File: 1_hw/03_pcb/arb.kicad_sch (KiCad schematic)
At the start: 0 parts

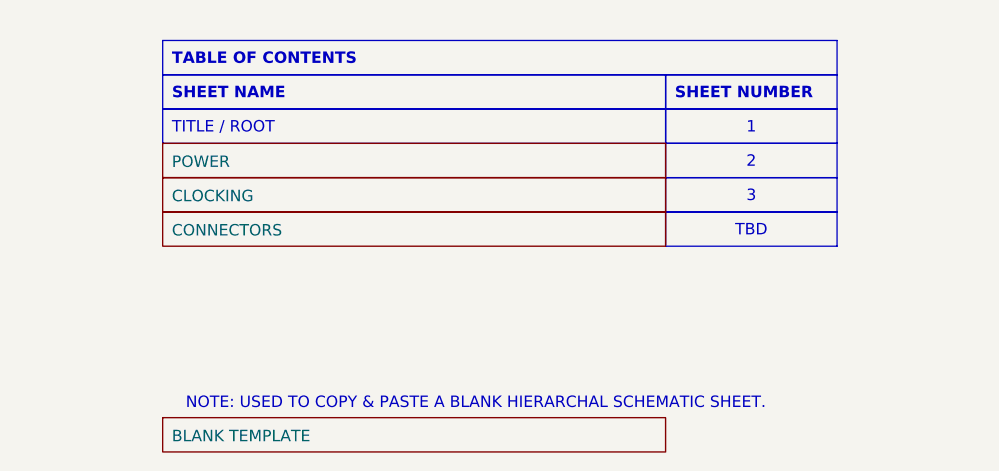
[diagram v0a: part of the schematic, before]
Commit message: FEAT: Modified Block Diagram. Added Pin Map Excel.
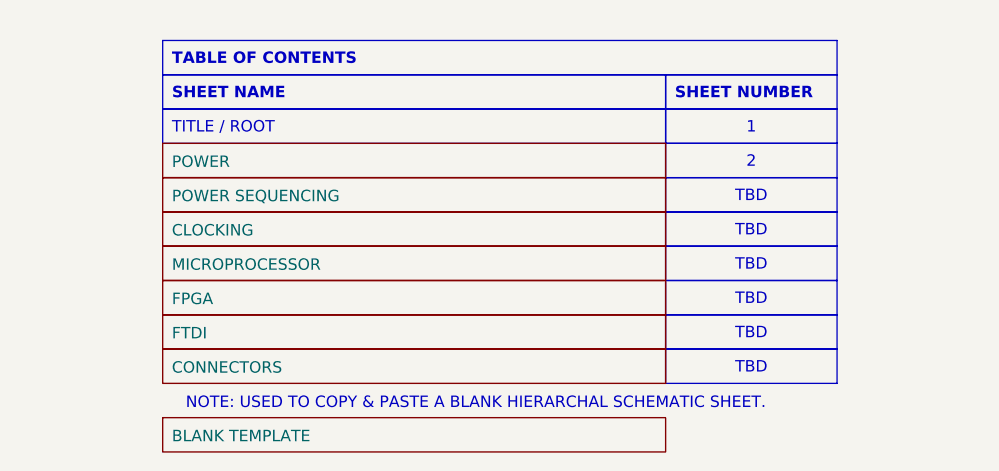
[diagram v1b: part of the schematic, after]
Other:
- added sheet FPGA (fpga.kicad_sch)
- added sheet FTDI (ftdi.kicad_sch)
- added sheet MICROPROCESSOR (microprocessor.kicad_sch)
- added sheet POWER SEQUENCING (power_seq.kicad_sch)
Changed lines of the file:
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@@
 		(rev "0.0.1")
 		(company "Tomasz Brzyzek")
-		(comment 1 "brzk.net")
+		(comment 1 "Stasia Brzyzek")
 	)
 	(text_box "2"
@@
 		)
 	)
-	(text_box "3"
-		(exclude_from_sim no)
-		(at 165.1 85.09 0)
+	(text_box "TBD"
+		(exclude_from_sim no)
+		(at 165.1 88.9 0)
 		(size 19.05 3.81)
 		(stroke
@@
 		)
 	)
+	(text_box "TBD"
+		(exclude_from_sim no)
+		(at 165.1 92.71 0)
+		(size 19.05 3.81)
+		(stroke
+			(width 0)
+			(type default)
+			(color 0 0 0 1)
+		)
+		(fill
+			(type none)
+		)
+		(effects
+			(font
+				(size 1.27 1.27)
+				(color 0 72 72 1)
+			)
+		)
+	)
 	(text_box "SHEET NAME"
 		(exclude_from_sim no)
@@
 	(text_box "TBD"
 		(exclude_from_sim no)
-		(at 165.1 88.9 0)
+		(at 165.1 104.14 0)
 		(size 19.05 3.81)
 		(stroke
@@
 		)
 	)
+	(text_box "TBD"
+		(exclude_from_sim no)
+		(at 165.1 100.33 0)
+		(size 19.05 3.81)
+		(stroke
+			(width 0)
+			(type default)
+			(color 0 0 0 1)
+		)
+		(fill
+			(type none)
+		)
+		(effects
+			(font
+				(size 1.27 1.27)
+				(color 0 72 72 1)
+			)
+		)
+	)
+	(text_box "TBD"
+		(exclude_from_sim no)
+		(at 165.1 85.09 0)
+		(size 19.05 3.81)
+		(stroke
+			(width 0)
+			(type default)
+			(color 0 0 0 1)
+		)
+		(fill
+			(type none)
+		)
+		(effects
+			(font
+				(size 1.27 1.27)
+				(color 0 72 72 1)
+			)
+		)
+	)
 	(text_box "NOTES:\n1.	TBD"
 		(exclude_from_sim no)
@@
 		)
 	)
+	(text_box "TBD"
+		(exclude_from_sim no)
+		(at 165.1 96.52 0)
+		(size 19.05 3.81)
+		(stroke
+			(width 0)
+			(type default)
+			(color 0 0 0 1)
+		)
+		(fill
+			(type none)
+		)
+		(effects
+			(font
+				(size 1.27 1.27)
+				(color 0 72 72 1)
+			)
+		)
+	)
 	(text_box "1"
 		(exclude_from_sim no)
@@
 			(font
 				(size 1.27 1.27)
+			)
+		)
+	)
+	(sheet
+		(at 109.22 92.71)
+		(size 55.88 3.81)
+		(stroke
+			(width 0.1524)
+			(type solid)
+			(color 0 0 0 1)
+		)
+		(fill
+			(color 0 0 0 0.0000)
+		)
+		(property "Sheetname" "MICROPROCESSOR"
+			(at 110.236 94.742 0)
+			(effects
+				(font
+					(size 1.27 1.27)
+				)
+				(justify left)
+			)
+		)
+		(property "Sheetfile" "microprocessor.kicad_sch"
+			(at 109.22 97.1046 0)
+			(effects
+				(font
+					(size 1.27 1.27)
+				)
+				(justify left top)
+				(hide yes)
+			)
+		)
+		(instances
+			(project "arb"
+				(path "/866ef9be-3b01-4288-a6e0-a2357aa17e50"
+					(page "5")
+				)
+			)
+		)
+	)
+	(sheet
+		(at 109.22 96.52)
+		(size 55.88 3.81)
+		(stroke
+			(width 0.1524)
+			(type solid)
+			(color 0 0 0 1)
+		)
+		(fill
+			(color 0 0 0 0.0000)
+		)
+		(property "Sheetname" "FPGA"
+			(at 110.236 98.552 0)
+			(effects
+				(font
+					(size 1.27 1.27)
+				)
+				(justify left)
+			)
+		)
+		(property "Sheetfile" "fpga.kicad_sch"
+			(at 109.22 100.9146 0)
+			(effects
+				(font
+					(size 1.27 1.27)
+				)
+				(justify left top)
+				(hide yes)
+			)
+		)
+		(instances
+			(project "arb"
+				(path "/866ef9be-3b01-4288-a6e0-a2357aa17e50"
+					(page "6")
+				)
 			)
 		)
@@
 			(color 0 0 0 0.0000)
 		)
+		(property "Sheetname" "POWER SEQUENCING"
+			(at 110.236 87.122 0)
+			(effects
+				(font
+					(size 1.27 1.27)
+				)
+				(justify left)
+			)
+		)
+		(property "Sheetfile" "power_seq.kicad_sch"
+			(at 109.22 89.4846 0)
+			(effects
+				(font
+					(size 1.27 1.27)
+				)
+				(justify left top)
+				(hide yes)
+			)
+		)
+		(instances
+			(project "arb"
+				(path "/866ef9be-3b01-4288-a6e0-a2357aa17e50"
+					(page "4")
+				)
+			)
+		)
+	)
+	(sheet
+		(at 109.22 88.9)
+		(size 55.88 3.81)
+		(stroke
+			(width 0.1524)
+			(type solid)
+			(color 0 0 0 1)
+		)
+		(fill
+			(color 0 0 0 0.0000)
+		)
 		(property "Sheetname" "CLOCKING"
-			(at 110.236 87.122 0)
+			(at 110.236 90.932 0)
 			(effects
 				(font
@@
 		)
 		(property "Sheetfile" "clocking.kicad_sch"
-			(at 109.22 89.4846 0)
+			(at 109.22 93.2946 0)
 			(effects
 				(font
@@
 				(path "/866ef9be-3b01-4288-a6e0-a2357aa17e50"
 					(page "3")
+				)
+			)
+		)
+	)
+	(sheet
+		(at 109.22 100.33)
+		(size 55.88 3.81)
+		(stroke
+			(width 0.1524)
+			(type solid)
+			(color 0 0 0 1)
+		)
+		(fill
+			(color 0 0 0 0.0000)
+		)
+		(property "Sheetname" "FTDI"
+			(at 110.236 102.362 0)
+			(effects
+				(font
+					(size 1.27 1.27)
+				)
+				(justify left)
+			)
+		)
+		(property "Sheetfile" "ftdi.kicad_sch"
+			(at 109.22 104.7246 0)
+			(effects
+				(font
+					(size 1.27 1.27)
+				)
+				(justify left top)
+				(hide yes)
+			)
+		)
+		(instances
+			(project "arb"
+				(path "/866ef9be-3b01-4288-a6e0-a2357aa17e50"
+					(page "7")
 				)
 			)
@@
 			(project "arb"
 				(path "/866ef9be-3b01-4288-a6e0-a2357aa17e50"
-					(page "4")
-				)
-			)
-		)
-	)
-	(sheet
-		(at 109.22 88.9)
+					(page "10")
+				)
+			)
+		)
+	)
+	(sheet
+		(at 109.22 104.14)
 		(size 55.88 3.81)
 		(stroke
@@
 		)
 		(property "Sheetname" "CONNECTORS"
-			(at 110.236 90.932 0)
+			(at 110.236 106.172 0)
 			(effects
 				(font
@@
 		)
 		(property "Sheetfile" "connectors.kicad_sch"
-			(at 109.22 93.2946 0)
-			(effects
-				(font
-					(size 1.27 1.27)
-				)
-				(justify left top)
-				(hide yes)
-			)
-		)
-		(instances
-			(project "arb"
-				(path "/866ef9be-3b01-4288-a6e0-a2357aa17e50"
-					(page "5")
-				)
-			)
+			(at 109.22 108.5346 0)
+			(effects
+				(font
+					(size 1.27 1.27)
+				)
+				(justify left top)
+				(hide yes)
+			)
+		)
+		(instances
+			(project "arb"
+				(path "/866ef9be-3b01-4288-a6e0-a2357aa17e50"
+					(page "9")
+				)
+			)

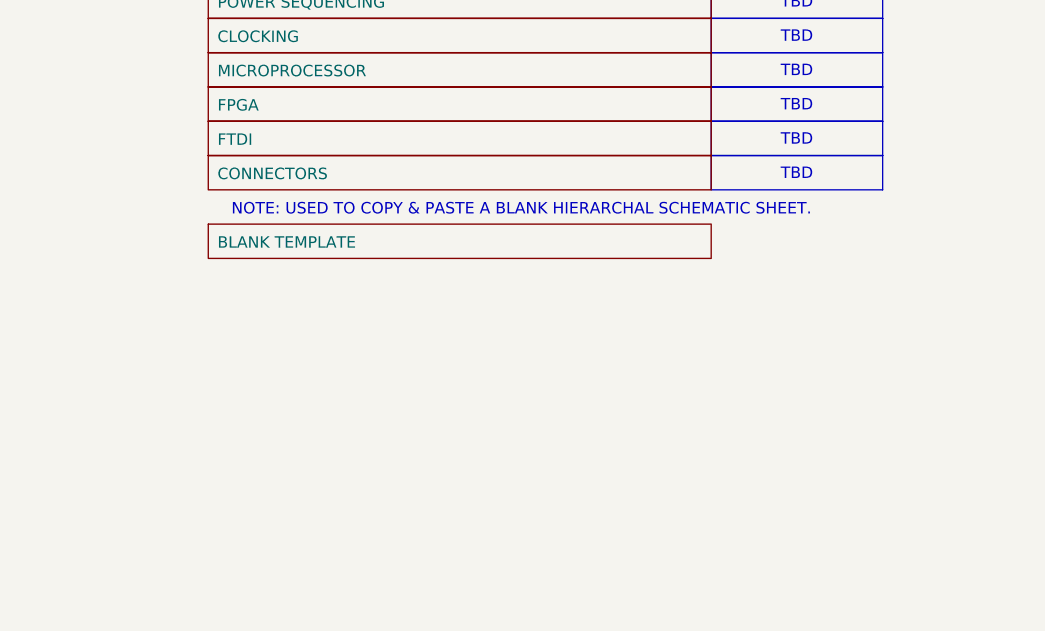
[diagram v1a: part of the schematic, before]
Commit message: FEAT: Added Level Translator Sheet, Symbols, added DAC and DDS to Schematic.
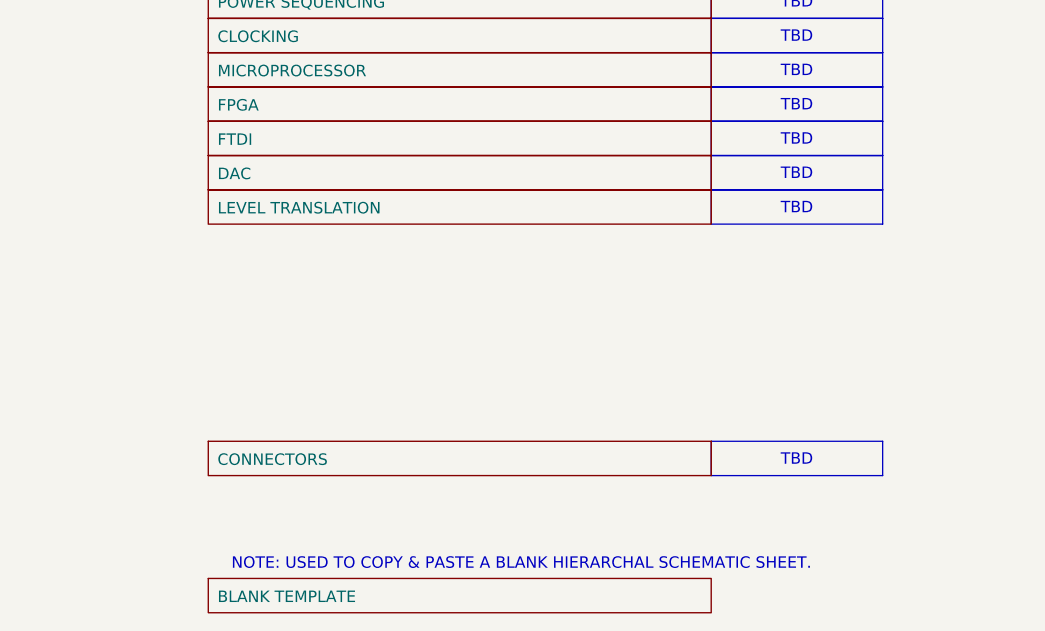
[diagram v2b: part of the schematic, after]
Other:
- added sheet DAC (dac.kicad_sch)
- added sheet LEVEL TRANSLATION (lvl_trns.kicad_sch)
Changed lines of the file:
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@@
+		)
+	)
+	(text_box "TBD"
+		(exclude_from_sim no)
+		(at 165.1 135.89 0)
+		(size 19.05 3.81)
+		(stroke
+			(width 0)
+			(type default)
+			(color 0 0 0 1)
+		)
+		(fill
+			(type none)
+		)
+		(effects
+			(font
+				(size 1.27 1.27)
+				(color 0 72 72 1)
+			)
+		)
+	)
+	(text_box "TBD"
+		(exclude_from_sim no)
+		(at 165.1 107.95 0)
+		(size 19.05 3.81)
+		(stroke
+			(width 0)
+			(type default)
+			(color 0 0 0 1)
+		)
+		(fill
+			(type none)
+		)
+		(effects
+			(font
+				(size 1.27 1.27)
+				(color 0 72 72 1)
+			)
 		)
 	)
@@
 	(text "NOTE: USED TO COPY & PASTE A BLANK HIERARCHAL SCHEMATIC SHEET."
 		(exclude_from_sim no)
-		(at 144.018 110.236 0)
+		(at 144.018 149.606 0)
 		(effects
 			(font
@@
 	)
 	(sheet
-		(at 109.22 111.76)
+		(at 109.22 104.14)
+		(size 55.88 3.81)
+		(stroke
+			(width 0.1524)
+			(type solid)
+			(color 0 0 0 1)
+		)
+		(fill
+			(color 0 0 0 0.0000)
+		)
+		(property "Sheetname" "DAC"
+			(at 110.236 106.172 0)
+			(effects
+				(font
+					(size 1.27 1.27)
+				)
+				(justify left)
+			)
+		)
+		(property "Sheetfile" "dac.kicad_sch"
+			(at 109.22 108.5346 0)
+			(effects
+				(font
+					(size 1.27 1.27)
+				)
+				(justify left top)
+				(hide yes)
+			)
+		)
+		(instances
+			(project "arb"
+				(path "/866ef9be-3b01-4288-a6e0-a2357aa17e50"
+					(page "8")
+				)
+			)
+		)
+	)
+	(sheet
+		(at 109.22 107.95)
+		(size 55.88 3.81)
+		(stroke
+			(width 0.1524)
+			(type solid)
+			(color 0 0 0 1)
+		)
+		(fill
+			(color 0 0 0 0.0000)
+		)
+		(property "Sheetname" "LEVEL TRANSLATION"
+			(at 110.236 109.982 0)
+			(effects
+				(font
+					(size 1.27 1.27)
+				)
+				(justify left)
+			)
+		)
+		(property "Sheetfile" "lvl_trns.kicad_sch"
+			(at 109.22 112.3446 0)
+			(effects
+				(font
+					(size 1.27 1.27)
+				)
+				(justify left top)
+				(hide yes)
+			)
+		)
+		(instances
+			(project "arb"
+				(path "/866ef9be-3b01-4288-a6e0-a2357aa17e50"
+					(page "9")
+				)
+			)
+		)
+	)
+	(sheet
+		(at 109.22 151.13)
 		(size 55.88 3.81)
 		(stroke
@@
 		)
 		(property "Sheetname" "BLANK TEMPLATE"
-			(at 110.236 113.792 0)
+			(at 110.236 153.162 0)
 			(effects
 				(font
@@
 		)
 		(property "Sheetfile" "blank_template.kicad_sch"
-			(at 109.22 116.1546 0)
-			(effects
-				(font
-					(size 1.27 1.27)
-				)
-				(justify left top)
-				(hide yes)
-			)
-		)
-		(instances
-			(project "arb"
-				(path "/866ef9be-3b01-4288-a6e0-a2357aa17e50"
-					(page "10")
-				)
-			)
-		)
-	)
-	(sheet
-		(at 109.22 104.14)
+			(at 109.22 155.5246 0)
+			(effects
+				(font
+					(size 1.27 1.27)
+				)
+				(justify left top)
+				(hide yes)
+			)
+		)
+		(instances
+			(project "arb"
+				(path "/866ef9be-3b01-4288-a6e0-a2357aa17e50"
+					(page "99")
+				)
+			)
+		)
+	)
+	(sheet
+		(at 109.22 135.89)
 		(size 55.88 3.81)
 		(stroke
@@
 		)
 		(property "Sheetname" "CONNECTORS"
-			(at 110.236 106.172 0)
+			(at 110.236 137.922 0)
 			(effects
 				(font
@@
 		)
 		(property "Sheetfile" "connectors.kicad_sch"
-			(at 109.22 108.5346 0)
-			(effects
-				(font
-					(size 1.27 1.27)
-				)
-				(justify left top)
-				(hide yes)
-			)
-		)
-		(instances
-			(project "arb"
-				(path "/866ef9be-3b01-4288-a6e0-a2357aa17e50"
-					(page "9")
-				)
-			)
+			(at 109.22 140.2846 0)
+			(effects
+				(font
+					(size 1.27 1.27)
+				)
+				(justify left top)
+				(hide yes)
+			)
+		)
+		(instances
+			(project "arb"
+				(path "/866ef9be-3b01-4288-a6e0-a2357aa17e50"
+					(page "20")
+				)
+			)

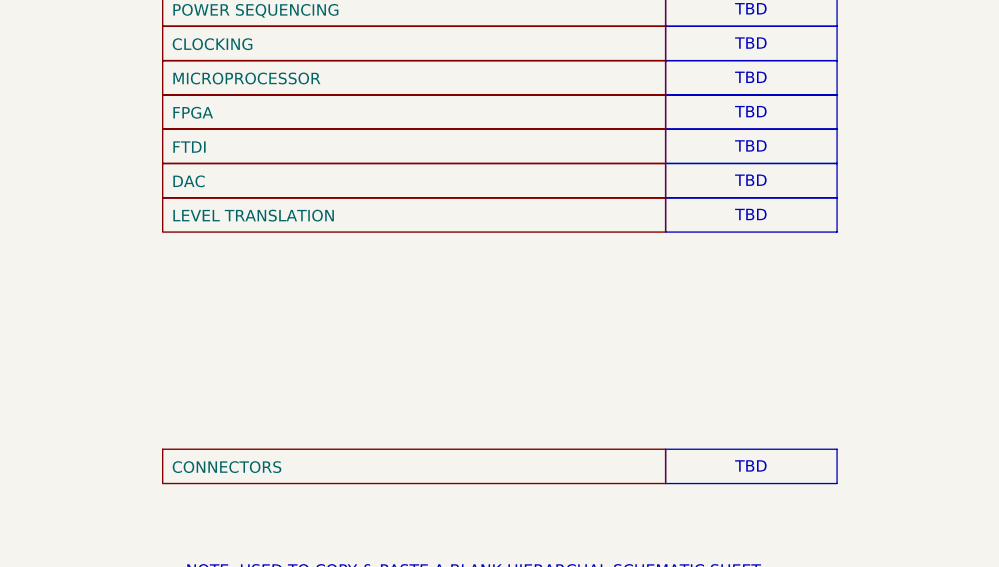
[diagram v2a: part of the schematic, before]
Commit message: FEAT: Simulated Analog Paths, added first stage analog amp to schematic.
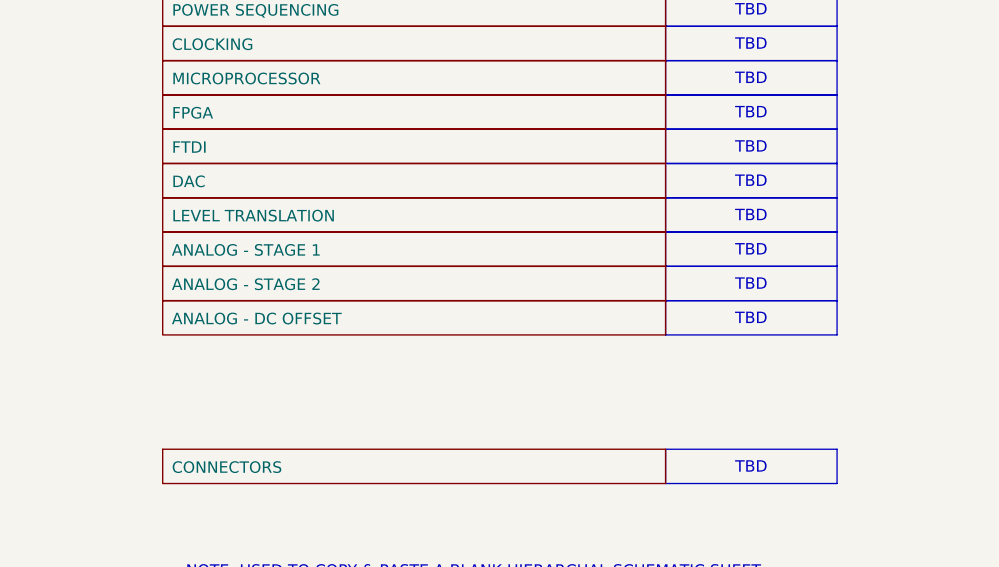
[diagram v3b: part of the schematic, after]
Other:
- added sheet ANALOG - DC OFFSET (analogdc.kicad_sch)
- added sheet ANALOG - STAGE 1 (analog1.kicad_sch)
- added sheet ANALOG - STAGE 2 (analog2.kicad_sch)
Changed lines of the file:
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@@
 		(rev "0.0.1")
 		(company "Tomasz Brzyzek")
-		(comment 1 "Stasia Brzyzek")
 	)
 	(text_box "2"
@@
 	(text_box "TBD"
 		(exclude_from_sim no)
+		(at 165.1 111.76 0)
+		(size 19.05 3.81)
+		(stroke
+			(width 0)
+			(type default)
+			(color 0 0 0 1)
+		)
+		(fill
+			(type none)
+		)
+		(effects
+			(font
+				(size 1.27 1.27)
+				(color 0 72 72 1)
+			)
+		)
+	)
+	(text_box "TBD"
+		(exclude_from_sim no)
 		(at 165.1 135.89 0)
 		(size 19.05 3.81)
@@
 		)
 	)
+	(text_box "TBD"
+		(exclude_from_sim no)
+		(at 165.1 119.38 0)
+		(size 19.05 3.81)
+		(stroke
+			(width 0)
+			(type default)
+			(color 0 0 0 1)
+		)
+		(fill
+			(type none)
+		)
+		(effects
+			(font
+				(size 1.27 1.27)
+				(color 0 72 72 1)
+			)
+		)
+	)
 	(text_box "INITIAL RELEASE"
 		(exclude_from_sim no)
@@
 		(exclude_from_sim no)
 		(at 165.1 77.47 0)
+		(size 19.05 3.81)
+		(stroke
+			(width 0)
+			(type default)
+			(color 0 0 0 1)
+		)
+		(fill
+			(type none)
+		)
+		(effects
+			(font
+				(size 1.27 1.27)
+				(color 0 72 72 1)
+			)
+		)
+	)
+	(text_box "TBD"
+		(exclude_from_sim no)
+		(at 165.1 115.57 0)
 		(size 19.05 3.81)
 		(stroke
@@
 	)
 	(sheet
+		(at 109.22 111.76)
+		(size 55.88 3.81)
+		(stroke
+			(width 0.1524)
+			(type solid)
+			(color 0 0 0 1)
+		)
+		(fill
+			(color 0 0 0 0.0000)
+		)
+		(property "Sheetname" "ANALOG - STAGE 1"
+			(at 110.236 113.792 0)
+			(effects
+				(font
+					(size 1.27 1.27)
+				)
+				(justify left)
+			)
+		)
+		(property "Sheetfile" "analog1.kicad_sch"
+			(at 109.22 116.1546 0)
+			(effects
+				(font
+					(size 1.27 1.27)
+				)
+				(justify left top)
+				(hide yes)
+			)
+		)
+		(instances
+			(project "arb"
+				(path "/866ef9be-3b01-4288-a6e0-a2357aa17e50"
+					(page "10")
+				)
+			)
+		)
+	)
+	(sheet
 		(at 109.22 81.28)
 		(size 55.88 3.81)
@@
 			(project "arb"
 				(path "/866ef9be-3b01-4288-a6e0-a2357aa17e50"
-					(page "4")
+					(page "3")
 				)
 			)
@@
 			(project "arb"
 				(path "/866ef9be-3b01-4288-a6e0-a2357aa17e50"
-					(page "3")
+					(page "4")
 				)
 			)
@@
 				)
 			)
+		)
+	)
+	(sheet
+		(at 109.22 119.38)
+		(size 55.88 3.81)
+		(stroke
+			(width 0.1524)
+			(type solid)
+			(color 0 0 0 1)
+		)
+		(fill
+			(color 0 0 0 0.0000)
+		)
+		(property "Sheetname" "ANALOG - DC OFFSET"
+			(at 110.236 121.412 0)
+			(effects
+				(font
+					(size 1.27 1.27)
+				)
+				(justify left)
+			)
+		)
+		(property "Sheetfile" "analogdc.kicad_sch"
+			(at 109.22 123.7746 0)
+			(effects
+				(font
+					(size 1.27 1.27)
+				)
+				(justify left top)
+				(hide yes)
+			)
+		)
+		(instances
+			(project "arb"
+				(path "/866ef9be-3b01-4288-a6e0-a2357aa17e50"
+					(page "12")
+				)
+			)
+		)
+	)
+	(sheet
+		(at 109.22 115.57)
+		(size 55.88 3.81)
+		(stroke
+			(width 0.1524)
+			(type solid)
+			(color 0 0 0 1)
+		)
+		(fill
+			(color 0 0 0 0.0000)
+		)
+		(property "Sheetname" "ANALOG - STAGE 2"
+			(at 110.236 117.602 0)
+			(effects
+				(font
+					(size 1.27 1.27)
+				)
+				(justify left)
+			)
+		)
+		(property "Sheetfile" "analog2.kicad_sch"
+			(at 109.22 119.9646 0)
+			(effects
+				(font
+					(size 1.27 1.27)
+				)
+				(justify left top)
+				(hide yes)
+			)
+		)
+		(instances
+			(project "arb"
+				(path "/866ef9be-3b01-4288-a6e0-a2357aa17e50"
+					(page "11")
+				)
+			)

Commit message: FEAT: Created Power Consumption Matrix.
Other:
- removed sheet LEVEL TRANSLATION
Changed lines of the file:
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@@
 	(text_box "TBD"
 		(exclude_from_sim no)
-		(at 165.1 111.76 0)
+		(at 165.1 107.95 0)
 		(size 19.05 3.81)
 		(stroke
@@
 		(exclude_from_sim no)
 		(at 165.1 135.89 0)
-		(size 19.05 3.81)
-		(stroke
-			(width 0)
-			(type default)
-			(color 0 0 0 1)
-		)
-		(fill
-			(type none)
-		)
-		(effects
-			(font
-				(size 1.27 1.27)
-				(color 0 72 72 1)
-			)
-		)
-	)
-	(text_box "TBD"
-		(exclude_from_sim no)
-		(at 165.1 107.95 0)
 		(size 19.05 3.81)
 		(stroke
@@
 	(text_box "TBD"
 		(exclude_from_sim no)
-		(at 165.1 119.38 0)
+		(at 165.1 115.57 0)
 		(size 19.05 3.81)
 		(stroke
@@
 	(text_box "TBD"
 		(exclude_from_sim no)
-		(at 165.1 115.57 0)
+		(at 165.1 111.76 0)
 		(size 19.05 3.81)
 		(stroke
@@
 	)
 	(sheet
-		(at 109.22 111.76)
+		(at 109.22 107.95)
 		(size 55.88 3.81)
 		(stroke
@@
 		)
 		(property "Sheetname" "ANALOG - STAGE 1"
-			(at 110.236 113.792 0)
+			(at 110.236 109.982 0)
 			(effects
 				(font
@@
 		)
 		(property "Sheetfile" "analog1.kicad_sch"
-			(at 109.22 116.1546 0)
+			(at 109.22 112.3446 0)
 			(effects
 				(font
@@
 	)
 	(sheet
-		(at 109.22 107.95)
-		(size 55.88 3.81)
-		(stroke
-			(width 0.1524)
-			(type solid)
-			(color 0 0 0 1)
-		)
-		(fill
-			(color 0 0 0 0.0000)
-		)
-		(property "Sheetname" "LEVEL TRANSLATION"
-			(at 110.236 109.982 0)
-			(effects
-				(font
-					(size 1.27 1.27)
-				)
-				(justify left)
-			)
-		)
-		(property "Sheetfile" "lvl_trns.kicad_sch"
-			(at 109.22 112.3446 0)
-			(effects
-				(font
-					(size 1.27 1.27)
-				)
-				(justify left top)
-				(hide yes)
-			)
-		)
-		(instances
-			(project "arb"
-				(path "/866ef9be-3b01-4288-a6e0-a2357aa17e50"
-					(page "9")
-				)
-			)
-		)
-	)
-	(sheet
 		(at 109.22 151.13)
 		(size 55.88 3.81)
@@
 	)
 	(sheet
-		(at 109.22 119.38)
+		(at 109.22 115.57)
 		(size 55.88 3.81)
 		(stroke
@@
 		)
 		(property "Sheetname" "ANALOG - DC OFFSET"
-			(at 110.236 121.412 0)
+			(at 110.236 117.602 0)
 			(effects
 				(font
@@
 		)
 		(property "Sheetfile" "analogdc.kicad_sch"
-			(at 109.22 123.7746 0)
+			(at 109.22 119.9646 0)
 			(effects
 				(font
@@
 	)
 	(sheet
-		(at 109.22 115.57)
+		(at 109.22 111.76)
 		(size 55.88 3.81)
 		(stroke
@@
 		)
 		(property "Sheetname" "ANALOG - STAGE 2"
-			(at 110.236 117.602 0)
+			(at 110.236 113.792 0)
 			(effects
 				(font
@@
 		)
 		(property "Sheetfile" "analog2.kicad_sch"
-			(at 109.22 119.9646 0)
-			(effects
-				(font
+			(at 109.22 116.1546 0)
+			(effects
+				(font
